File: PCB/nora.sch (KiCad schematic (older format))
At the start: 208 parts, among them J1 USB_C_Receptacle_USB2.0, J2 Conn_01x03, J3 Conn_01x02, J5 Conn_02x03_Odd_Even, U1 ATmega32U4-MU, U2 24LC64, U3 ATmega32U4-AU-Dummy, Y1 16MHz

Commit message: ファイル名変更と配線途中
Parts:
- removed J2: Conn_01x03, Connector_PinHeader_2.54mm:PinHeader_1x03_P2.54mm_Vertical, symbol Connector_Generic:Conn_01x03
- removed J? (x2): Conn_01x05, symbol Connector_Generic:Conn_01x05
- added EXT_R0, EXT_R1, EXT_R2, EXT_R3, EXT_R4, EXT_R5, EXT_R6, EXT_R7, EXT_R8, EXT_R9: Conn_01x01, TestPoint:TestPoint_THTPad_D1.5mm_Drill0.7mm, symbol Connector_Generic:Conn_01x01
- added U4: Pico, MCU_RaspberryPi_and_Boards:RPi_Pico_TH_no_NPTH_SWD_less_Silk, symbol MCU_RaspberryPi_and_Boards:Pico
- U3: symbol choc_in_60:ATmega32U4-AU-Dummy -> nora:ATmega32U4-AU-Dummy
- renumbered ReservePin to ReservePin1
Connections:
- wire segments 470 -> 475
- no-connect marks 4 -> 28

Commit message: 配線つなぎ終わりだけど、つないだだけ状態
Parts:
- removed U4: Pico, MCU_RaspberryPi_and_Boards:RPi_Pico_TH_no_NPTH_SWD_less_Silk, symbol MCU_RaspberryPi_and_Boards:Pico
- D1, D11, D12, D13, D14, D15, D16, D17, D18, D19, D2, D20, D21, D22, D23, D25, D26, D27, D28, D29, D3, D30, D31, D32, D33, D35, D36, D37, D38, D39, D4, D40, D41, D42, D43, D45, D46, D47, D48, D49, D5, D50, D51, D52, D53, D54, D55, D56, D57, D58, D59, D6, D60, D61, D62, D63, D64, D65, D66, D67, D68, D69, D7, D70, D71, D72, D73, D74, D75, D76, D77, D78, D79, D8, D9: footprint Diode_SMD:D_SOD-123 -> locallib:D_SOD-123_Refelence@Left
- renumbered ReservePin1 to Ext_PC6
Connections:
- net col1: now also U1.21 (PD3), U3.21 (PD3); no longer U1.22 (PD5), U3.22 (PD5)
- net col2: now also U1.22 (PD5), U3.22 (PD5); no longer U1.29 (PB5), U3.29 (PB5)
- net col3: now also U1.25 (PD4), U3.25 (PD4); no longer U1.27 (PD7), U3.27 (PD7)
- net col4: now also U1.26 (PD6), U3.26 (PD6); no longer U1.21 (PD3), U3.21 (PD3)
- net col5: now also U1.27 (PD7), U3.27 (PD7); no longer U1.25 (PD4), U3.25 (PD4)
- net col7: now also U1.29 (PB5), U3.29 (PB5); no longer U1.26 (PD6), U3.26 (PD6)
- net row8: now also U1.32 (PC7), U3.32 (PC7); no longer U1.30 (PB6), U3.30 (PB6)
- net row9: now also U1.30 (PB6), U3.30 (PB6); no longer U1.32 (PC7), U3.32 (PC7)
- no-connect marks 28 -> 5

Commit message: ロゴ追加
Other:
- moved on the sheet: U2
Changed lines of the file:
@@
 	-1   0    0    1
 $EndComp
-Text GLabel 9750 8625 2    50   Input ~ 0
+Text GLabel 9300 8775 2    50   Input ~ 0
 SDA
-Text GLabel 9750 8725 2    50   Input ~ 0
+Text GLabel 9300 8875 2    50   Input ~ 0
 SCL
-Connection ~ 8950 9025
+Connection ~ 8500 9175
 Wire Wire Line
-	8950 9025 8950 9125
+	8500 9175 8500 9275
 Wire Wire Line
-	8950 8425 9350 8425
+	8500 8575 8900 8575
 Wire Wire Line
-	8950 8325 8950 8425
+	8500 8475 8500 8575
 $Comp
 L power:+5V #PWR0102
 U 1 1 60AF154D
-P 8950 8325
-F 0 "#PWR0102" H 8950 8175 50  0001 C CNN
-F 1 "+5V" H 8950 8465 50  0000 C CNN
-F 2 "" H 8950 8325 50  0001 C CNN
-F 3 "" H 8950 8325 50  0001 C CNN
-	1    8950 8325
+P 8500 8475
+F 0 "#PWR0102" H 8500 8325 50  0001 C CNN
+F 1 "+5V" H 8500 8615 50  0000 C CNN
+F 2 "" H 8500 8475 50  0001 C CNN
+F 3 "" H 8500 8475 50  0001 C CNN
+	1    8500 8475
 	1    0    0    -1
 $EndComp
 Wire Wire Line
-	9750 9025 9350 9025
+	9300 9175 8900 9175
 Wire Wire Line
-	9750 8825 9750 9025
-Connection ~ 9350 9025
+	9300 8975 9300 9175
+Connection ~ 8900 9175
 Wire Wire Line
-	8950 8825 8950 9025
-Connection ~ 8950 8825
+	8500 8975 8500 9175
+Connection ~ 8500 8975
 Wire Wire Line
-	8950 8725 8950 8825
-Connection ~ 8950 8725
+	8500 8875 8500 8975
+Connection ~ 8500 8875
 Wire Wire Line
-	8950 9025 9350 9025
+	8500 9175 8900 9175
 Wire Wire Line
-	8950 8625 8950 8725
+	8500 8775 8500 8875
 $Comp
 L power:GND #PWR0101
 U 1 1 60B24F18
-P 8950 9125
-F 0 "#PWR0101" H 8950 8875 50  0001 C CNN
-F 1 "GND" H 8950 8975 50  0000 C CNN
-F 2 "" H 8950 9125 50  0001 C CNN
-F 3 "" H 8950 9125 50  0001 C CNN
-	1    8950 9125
+P 8500 9275
+F 0 "#PWR0101" H 8500 9025 50  0001 C CNN
+F 1 "GND" H 8500 9125 50  0000 C CNN
+F 2 "" H 8500 9275 50  0001 C CNN
+F 3 "" H 8500 9275 50  0001 C CNN
+	1    8500 9275
 	1    0    0    -1
 $EndComp
@@
 L Memory_EEPROM:24LC64 U2
 U 1 1 60AF01F9
-P 9350 8725
-F 0 "U2" H 9350 9206 50  0000 C CNN
-F 1 "24LC64" H 9350 9115 50  0000 C CNN
-F 2 "Package_SO:SO-8_3.9x4.9mm_P1.27mm" H 9350 8725 50  0001 C CNN
-F 3 "http://ww1.microchip.com/downloads/en/DeviceDoc/21189f.pdf" H 9350 8725 50  0001 C CNN
-F 4 "C79988" H 9350 8725 50  0001 C CNN "LCSC"
-	1    9350 8725
+P 8900 8875
+F 0 "U2" H 8900 9356 50  0000 C CNN
+F 1 "24LC64" H 8900 9265 50  0000 C CNN
+F 2 "Package_SO:SO-8_3.9x4.9mm_P1.27mm" H 8900 8875 50  0001 C CNN
+F 3 "http://ww1.microchip.com/downloads/en/DeviceDoc/21189f.pdf" H 8900 8875 50  0001 C CNN
+F 4 "C79988" H 8900 8875 50  0001 C CNN "LCSC"
+	1    8900 8875
 	1    0    0    -1
 $EndComp
@@
 Text Notes 12425 7825 0    100  ~ 20
 USB
-Text Notes 8850 8125 0    100  ~ 20
+Text Notes 8400 8275 0    100  ~ 20
 EEPROM
 Text Notes 10375 8250 0    100  ~ 20
@@
 Text GLabel 18075 3175 2    50   Input ~ 0
 SDA
-Text GLabel 18075 2775 2    50   Input ~ 0
-Reserve_pin
 Text GLabel 18075 3375 2    50   Input ~ 0
 col1
@@
 Text GLabel 15325 3275 2    50   Input ~ 0
 row2
+Text GLabel 18075 2775 2    50   Input ~ 0
+Reserve_pin
 $EndSCHEMATC

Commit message: スイッチのMill-Maxソケット対応
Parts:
- SW_3, SW_37, SW_71, SW_77, SW_78: footprint Keebio-Parts:Kailh-PG1350-1u-MBK-WithKeyName -> Keebio-Parts:Kailh-PG1350-1u-MBK-WithKeyName-MillMax
- SW_54: footprint Keebio-Parts:Kailh-PG1350-1.5u-MBK-WithKeyName -> Keebio-Parts:Kailh-PG1350-1.5u-MBK-WithKeyName-MillMax
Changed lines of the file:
@@
 F 0 "SW_3" H 1175 5535 50  0000 C CNN
 F 1 "SFT1u" H 1175 5444 50  0000 C CNN
-F 2 "Keebio-Parts:Kailh-PG1350-1u-MBK-WithKeyName" H 1175 5450 50  0001 C CNN
+F 2 "Keebio-Parts:Kailh-PG1350-1u-MBK-WithKeyName-MillMax" H 1175 5450 50  0001 C CNN
 F 3 "~" H 1175 5450 50  0001 C CNN
 	1    1175 5250
@@
 F 0 "SW_37" H 5725 4285 50  0000 C CNN
 F 1 "H" H 5725 4194 50  0000 C CNN
-F 2 "Keebio-Parts:Kailh-PG1350-1u-MBK-WithKeyName" H 5725 4200 50  0001 C CNN
+F 2 "Keebio-Parts:Kailh-PG1350-1u-MBK-WithKeyName-MillMax" H 5725 4200 50  0001 C CNN
 F 3 "~" H 5725 4200 50  0001 C CNN
 	1    5725 4000
@@
 F 0 "SW_54" H 7675 6785 50  0000 C CNN
 F 1 "RGUI_1.5u" H 7675 6694 50  0000 C CNN
-F 2 "Keebio-Parts:Kailh-PG1350-1.5u-MBK-WithKeyName" H 7675 6700 50  0001 C CNN
+F 2 "Keebio-Parts:Kailh-PG1350-1.5u-MBK-WithKeyName-MillMax" H 7675 6700 50  0001 C CNN
 F 3 "~" H 7675 6700 50  0001 C CNN
 	1    7675 6500
@@
 F 0 "SW_71" H 10275 3035 50  0000 C CNN
 F 1 "Num_8" H 10275 2944 50  0000 C CNN
-F 2 "Keebio-Parts:Kailh-PG1350-1u-MBK-WithKeyName" H 10275 2950 50  0001 C CNN
+F 2 "Keebio-Parts:Kailh-PG1350-1u-MBK-WithKeyName-MillMax" H 10275 2950 50  0001 C CNN
 F 3 "~" H 10275 2950 50  0001 C CNN
 	1    10275 2750
@@
 F 0 "SW_77" H 10925 4285 50  0000 C CNN
 F 1 "Num_6" H 10925 4194 50  0000 C CNN
-F 2 "Keebio-Parts:Kailh-PG1350-1u-MBK-WithKeyName" H 10925 4200 50  0001 C CNN
+F 2 "Keebio-Parts:Kailh-PG1350-1u-MBK-WithKeyName-MillMax" H 10925 4200 50  0001 C CNN
 F 3 "~" H 10925 4200 50  0001 C CNN
 	1    10925 4000
@@
 F 0 "SW_78" H 10925 5535 50  0000 C CNN
 F 1 "Num_3" H 10925 5444 50  0000 C CNN
-F 2 "Keebio-Parts:Kailh-PG1350-1u-MBK-WithKeyName" H 10925 5450 50  0001 C CNN
+F 2 "Keebio-Parts:Kailh-PG1350-1u-MBK-WithKeyName-MillMax" H 10925 5450 50  0001 C CNN
 F 3 "~" H 10925 5450 50  0001 C CNN
 	1    10925 5250

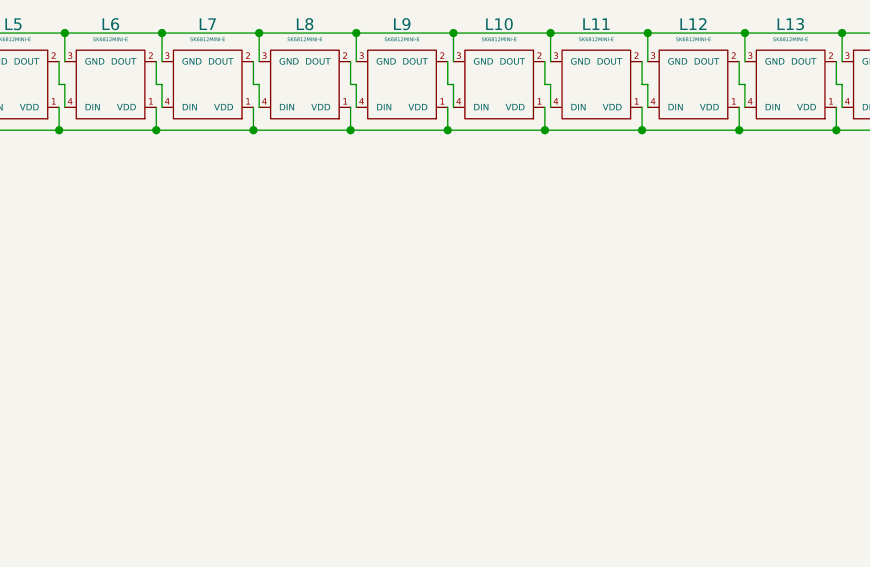
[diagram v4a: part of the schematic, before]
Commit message: Mill-Maxソケットの半田付け練習用を追加
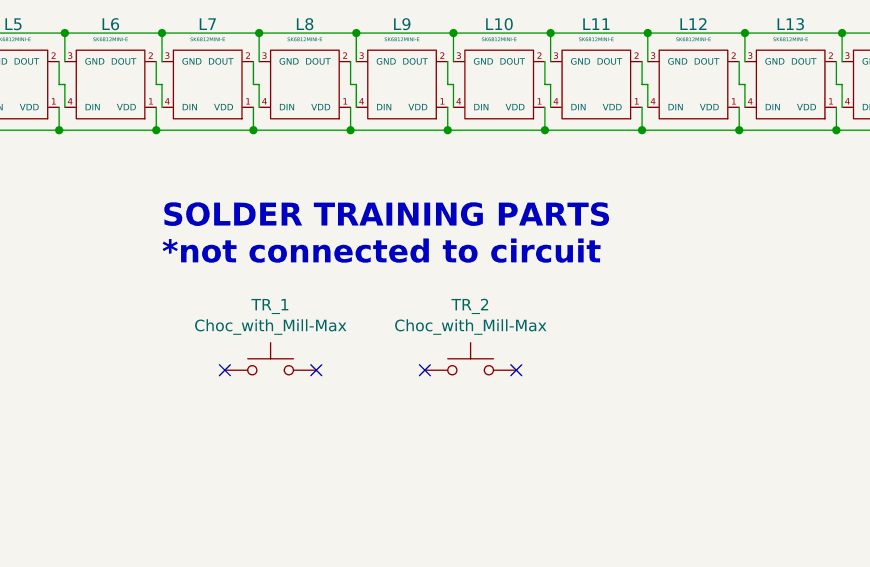
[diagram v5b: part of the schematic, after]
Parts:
- added TR_1, TR_2: Choc_with_Mill-Max, Keebio-Parts:Kailh-PG1350-1u-MBK-WithKeyName-MillMax, symbol Switch:SW_Push
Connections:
- no-connect marks 5 -> 9
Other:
- note added: "SOLDER TRAINING PARTS\n*not connected to circuit"
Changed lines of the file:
@@
 Text GLabel 18075 2775 2    50   Input ~ 0
 Reserve_pin
+Text Notes 3575 9675 0    100  ~ 20
+SOLDER TRAINING PARTS\n*not connected to circuit
+$Comp
+L Switch:SW_Push TR_1
+U 1 1 61AC4D56
+P 4050 10125
+F 0 "TR_1" H 4050 10410 50  0000 C CNN
+F 1 "Choc_with_Mill-Max" H 4050 10319 50  0000 C CNN
+F 2 "Keebio-Parts:Kailh-PG1350-1u-MBK-WithKeyName-MillMax" H 4050 10325 50  0001 C CNN
+F 3 "~" H 4050 10325 50  0001 C CNN
+	1    4050 10125
+	1    0    0    -1
+$EndComp
+$Comp
+L Switch:SW_Push TR_2
+U 1 1 61B4579B
+P 4925 10125
+F 0 "TR_2" H 4925 10410 50  0000 C CNN
+F 1 "Choc_with_Mill-Max" H 4925 10319 50  0000 C CNN
+F 2 "Keebio-Parts:Kailh-PG1350-1u-MBK-WithKeyName-MillMax" H 4925 10325 50  0001 C CNN
+F 3 "~" H 4925 10325 50  0001 C CNN
+	1    4925 10125
+	1    0    0    -1
+$EndComp
+NoConn ~ 4250 10125
+NoConn ~ 3850 10125
+NoConn ~ 4725 10125
+NoConn ~ 5125 10125
 $EndSCHEMATC

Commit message: 基板とSWプレートの製造データを用意
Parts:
- D1, D11, D12, D13, D14, D15, D16, D17, D18, D19, D2, D20, D21, D22, D23, D25, D26, D27, D28, D29, D3, D30, D31, D32, D33, D35, D36, D37, D38, D39, D4, D40, D41, D42, D43, D45, D46, D47, D48, D49, D5, D50, D51, D52, D53, D54, D55, D56, D57, D58, D59, D6, D60, D61, D62, D63, D64, D65, D66, D67, D68, D69, D7, D70, D71, D72, D73, D74, D75, D76, D77, D78, D79, D8, D9: LCSC (none) -> C81598
- U3: LCSC (none) -> C44854

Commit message: PICO対応
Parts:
- added J2: Conn_01x04, Connector_PinHeader_2.54mm:PinHeader_1x04_P2.54mm_Vertical, symbol Connector_Generic:Conn_01x04
- added JP1, JP2: SolderJumper_2_Open, Jumper:SolderJumper-2_P1.3mm_Open_RoundedPad1.0x1.5mm, symbol Jumper:SolderJumper_2_Open
- added JP3: SolderJumper_3_Open, Jumper:SolderJumper-3_P1.3mm_Open_RoundedPad1.0x1.5mm, symbol Jumper:SolderJumper_3_Open
- added U4: Pico, MCU_RaspberryPi_and_Boards:RPi_Pico_TH_no_NPTH_SWD_less_Silk_NoCrtYd, symbol nora:Pico_dummy
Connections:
- net +5V: now also JP3.3 (B); no longer L1.1 (VDD), L10.1 (VDD), L11.1 (VDD), L12.1 (VDD), L13.1 (VDD), L14.1 (VDD), L15.1 (VDD), L16.1 (VDD), L2.1 (VDD), L3.1 (VDD), L4.1 (VDD), L5.1 (VDD), L6.1 (VDD), L7.1 (VDD), L8.1 (VDD), L9.1 (VDD)
- net GND: now also U4.13 (GND), U4.18 (GND), U4.23 (GND), U4.28 (GND), U4.3 (GND), U4.38 (GND), U4.8 (GND)
- net LED: now also U4.34 (GPIO28_ADC2)
- net SCL: now also JP2.2 (B), U4.2 (GPIO1); no longer R9.2
- net SDA: now also JP1.2 (B), U4.1 (GPIO0); no longer R8.2
- net col0: now also U4.4 (GPIO2)
- net col1: now also U4.5 (GPIO3)
- net col2: now also U4.6 (GPIO4)
- net col3: now also U4.7 (GPIO5)
- net col4: now also U4.16 (GPIO12)
- net col5: now also U4.17 (GPIO13)
- net col6: now also U4.19 (GPIO14)
- net col7: now also U4.20 (GPIO15)
- net row0: now also U4.9 (GPIO6)
- net row1: now also U4.32 (GPIO27_ADC1)
- net row2: now also U4.29 (GPIO22)
- net row3: now also U4.25 (GPIO19)
- net row4: now also U4.22 (GPIO17)
- net row5: now also U4.10 (GPIO7)
- net row6: now also U4.31 (GPIO26_ADC0)
- net row7: now also U4.27 (GPIO21)
- net row8: now also U4.24 (GPIO18)
- net row9: now also U4.21 (GPIO16)
- new net: JP1.1 (A), R8.2
- new net: JP2.1 (A), R9.2
- new net: JP3.2 (C), L1.1 (VDD), L10.1 (VDD), L11.1 (VDD), L12.1 (VDD), L13.1 (VDD), L14.1 (VDD), L15.1 (VDD), L16.1 (VDD), L2.1 (VDD), L3.1 (VDD), L4.1 (VDD), L5.1 (VDD), L6.1 (VDD), L7.1 (VDD), L8.1 (VDD), L9.1 (VDD)
- new net PICO_10: J2.3 (Pin_3), U4.14 (GPIO10)
- new net PICO_11: J2.4 (Pin_4), U4.15 (GPIO11)
- new net PICO_8: J2.1 (Pin_1), U4.11 (GPIO8)
- new net PICO_9: J2.2 (Pin_2), U4.12 (GPIO9)
- new net PICO_VBUS: JP3.1 (A), U4.40 (VBUS)
- no-connect marks 9 -> 19
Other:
- moved on the sheet: J3, R8, R9

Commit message: 単純にHotswapのフットプリントへ置き換えて考え中
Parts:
- SW_1, SW_10, SW_11, SW_12, SW_13, SW_15, SW_16, SW_17, SW_18, SW_19, SW_2, SW_20, SW_21, SW_22, SW_23, SW_25, SW_26, SW_27, SW_28, SW_30, SW_31, SW_32, SW_33, SW_35, SW_36, SW_38, SW_4, SW_40, SW_41, SW_42, SW_43, SW_45, SW_46, SW_47, SW_48, SW_49, SW_5, SW_50, SW_51, SW_52, SW_53, SW_55, SW_56, SW_57, SW_58, SW_59, SW_60, SW_63, SW_64, SW_65, SW_66, SW_67, SW_68, SW_69, SW_70, SW_72, SW_73, SW_74, SW_75, SW_76, SW_79, SW_8, SW_9: footprint Keebio-Parts:Kailh-PG1350-1u-MBK-WithKeyName -> keyswitches:Kailh_socket_PG1350
- SW_14, SW_6, SW_61, SW_62: footprint Keebio-Parts:Kailh-PG1350-1.5u-MBK-WithKeyName -> keyswitches:Kailh_socket_PG1350
- SW_29, SW_39: footprint Keebio-Parts:Kailh-PG1350-2u-MBK-WithKeyName -> keyswitches:Kailh_socket_PG1350
- SW_3, SW_37, SW_71, SW_77, SW_78: footprint Keebio-Parts:Kailh-PG1350-1u-MBK-WithKeyName-MillMax -> keyswitches:Kailh_socket_PG1350
- SW_54: footprint Keebio-Parts:Kailh-PG1350-1.5u-MBK-WithKeyName-MillMax -> keyswitches:Kailh_socket_PG1350
- SW_7: footprint Keebio-Parts:Kailh-PG1350-1.5u-MBK-WithKeyName-NoClickHole -> keyswitches:Kailh_socket_PG1350
